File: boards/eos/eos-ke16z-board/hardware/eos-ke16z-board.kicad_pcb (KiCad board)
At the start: 2 copper layers, 68.6 x 53.3 mm, 67 parts, among them J1 USB-C, J2 SWD, J3 D8-SCL, J4 D0-D7, J5 POWER, J6 A0-A5, J7 EXT, Q1 AO3400A, Q2 AO3400A, Q3 AO3400A, SW1 RESET, SW2 USER1, SW3 USER2, U1 SP0503BAHTG, U2 CP2102N-A02-GQFN20, U3 AP7361C-33, U4 MKE16Z64VLF4, Y1 8MHz

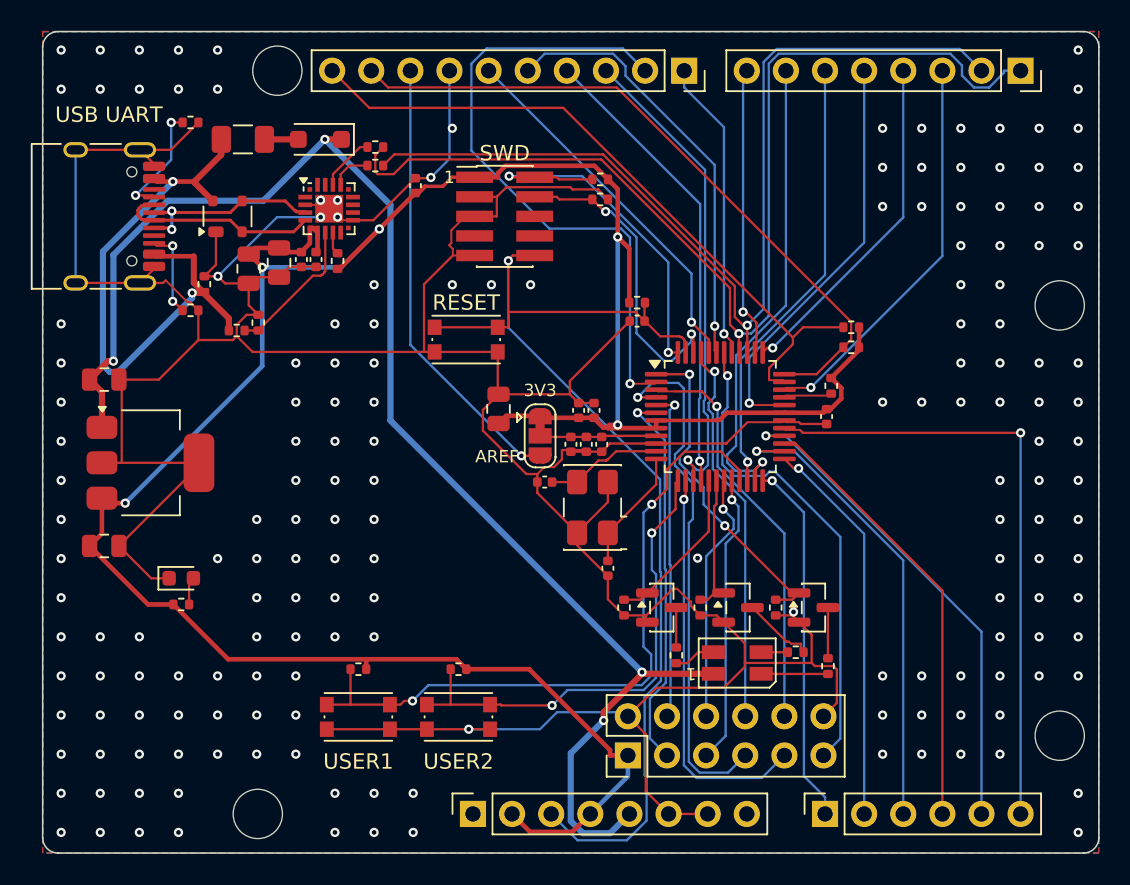
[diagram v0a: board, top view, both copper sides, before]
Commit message: fix(boards): rebuild the ten boards made before the no-via-in-pad rule (#55)
PR #64's generator keeps vias out of surface pads (a chip's exposed pad
aside) and 0.1 mm from their own net's pads. Ten boards on master were built
before that rule and had 34 pads with a via in or beside them. They are
rebuilt with the same generator: ATmega328P, RA2E1, KE16Z, KL25, STM32 64,
ESP32 DevKit, Learn RP2350, LPC55S69, CM4 Base and CM5 Base. Each builds at
ERC 0, DRC errors 0, unconnected 0 and parity 0, with the same parts, values,
nets and positions and the same DRC warnings as before.

Where the router could no longer close a short link without a via in a pad,
or left a ground pad without a good path to a via, the design files use
routing options only: priority routes, fanout_first, ground_vias, and a
bottom-layer router keep-out under KL25's crystal (so RESET_b no longer runs
under it). ViaInPadTest drops BUILT_BEFORE_THE_RULE; it now allows only Learn
RP2350's two Raspberry Pi reference vias, named by position. READMEs, TASKS
and CHANGELOG follow the rebuilt copper. Independent verification: three
rounds; the owner adopted a two-layer pour-island criterion (TASKS.md).

Part of #55.
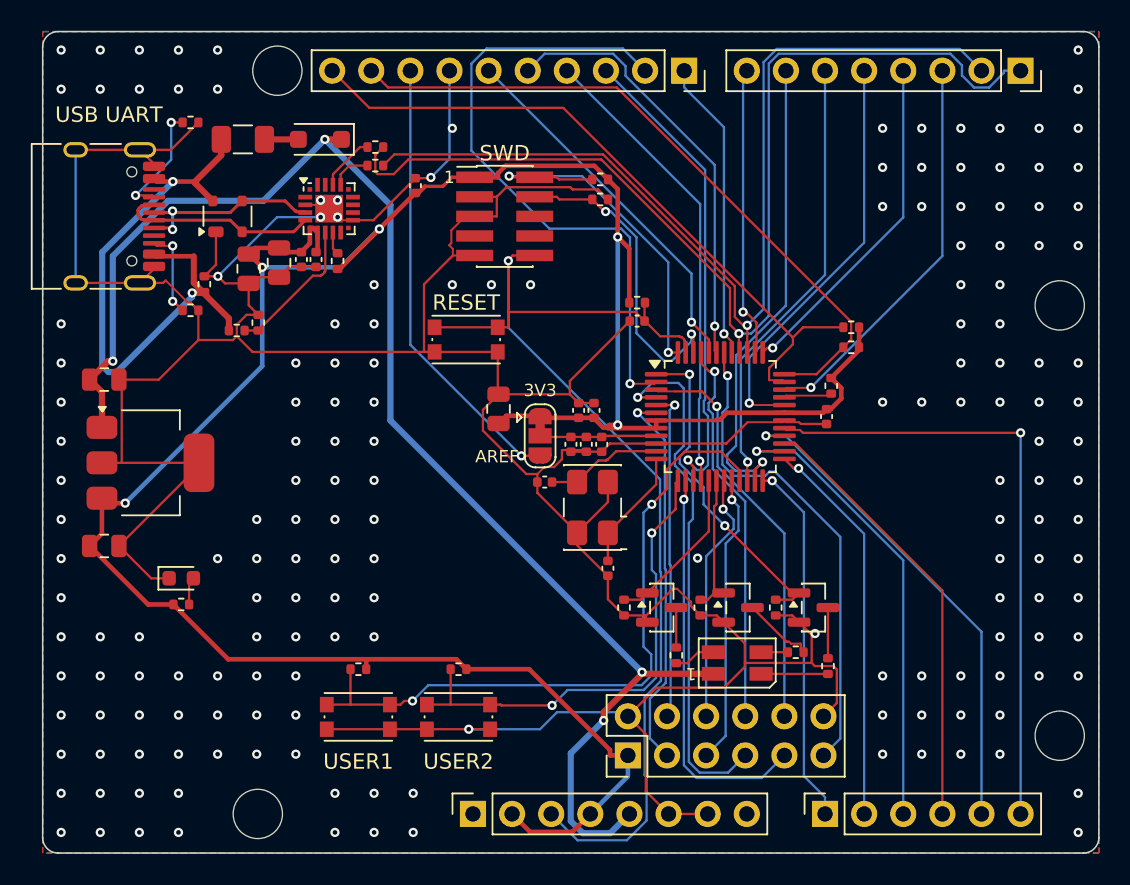
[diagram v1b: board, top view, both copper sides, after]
